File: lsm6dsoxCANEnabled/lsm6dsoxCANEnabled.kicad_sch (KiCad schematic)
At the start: 29 parts, among them J1 CANH and CANL, J2 GPIO, J3 Power, SW1 Nrst, SW2 BOOT0 selector, U2 TJA1051T, U3 STM32F103C8Tx, U4 AMS1117CD-3.3, Y1 Crystal_GND24

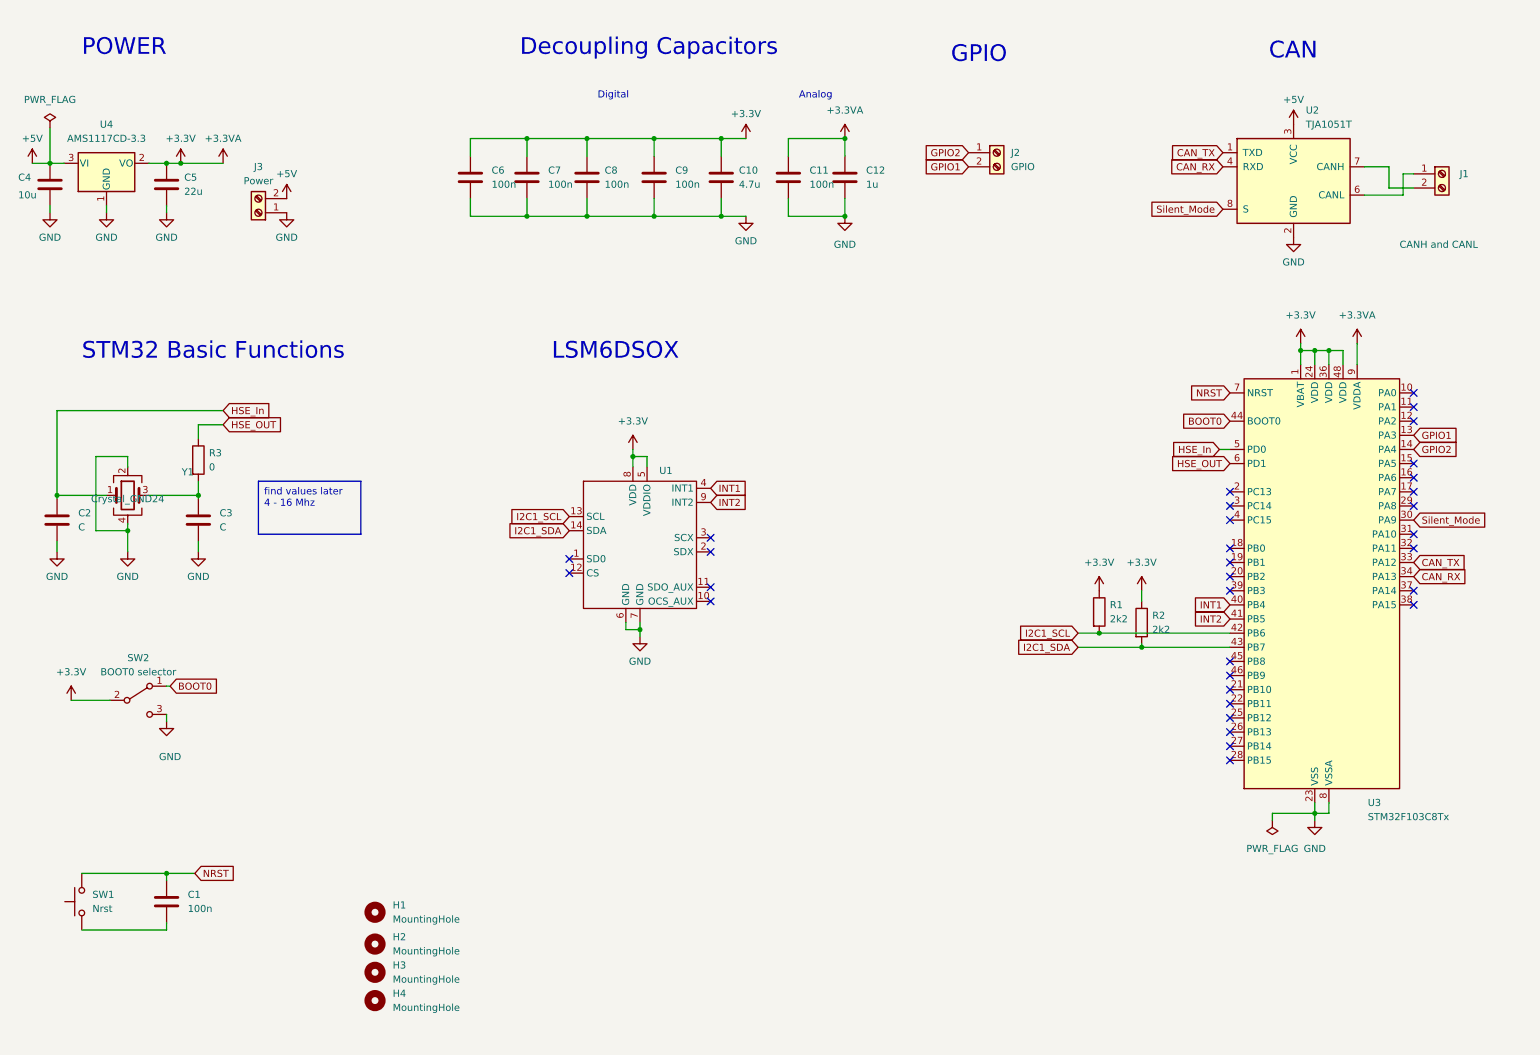
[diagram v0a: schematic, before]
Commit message: Started pcb with component placement and physical size constraints
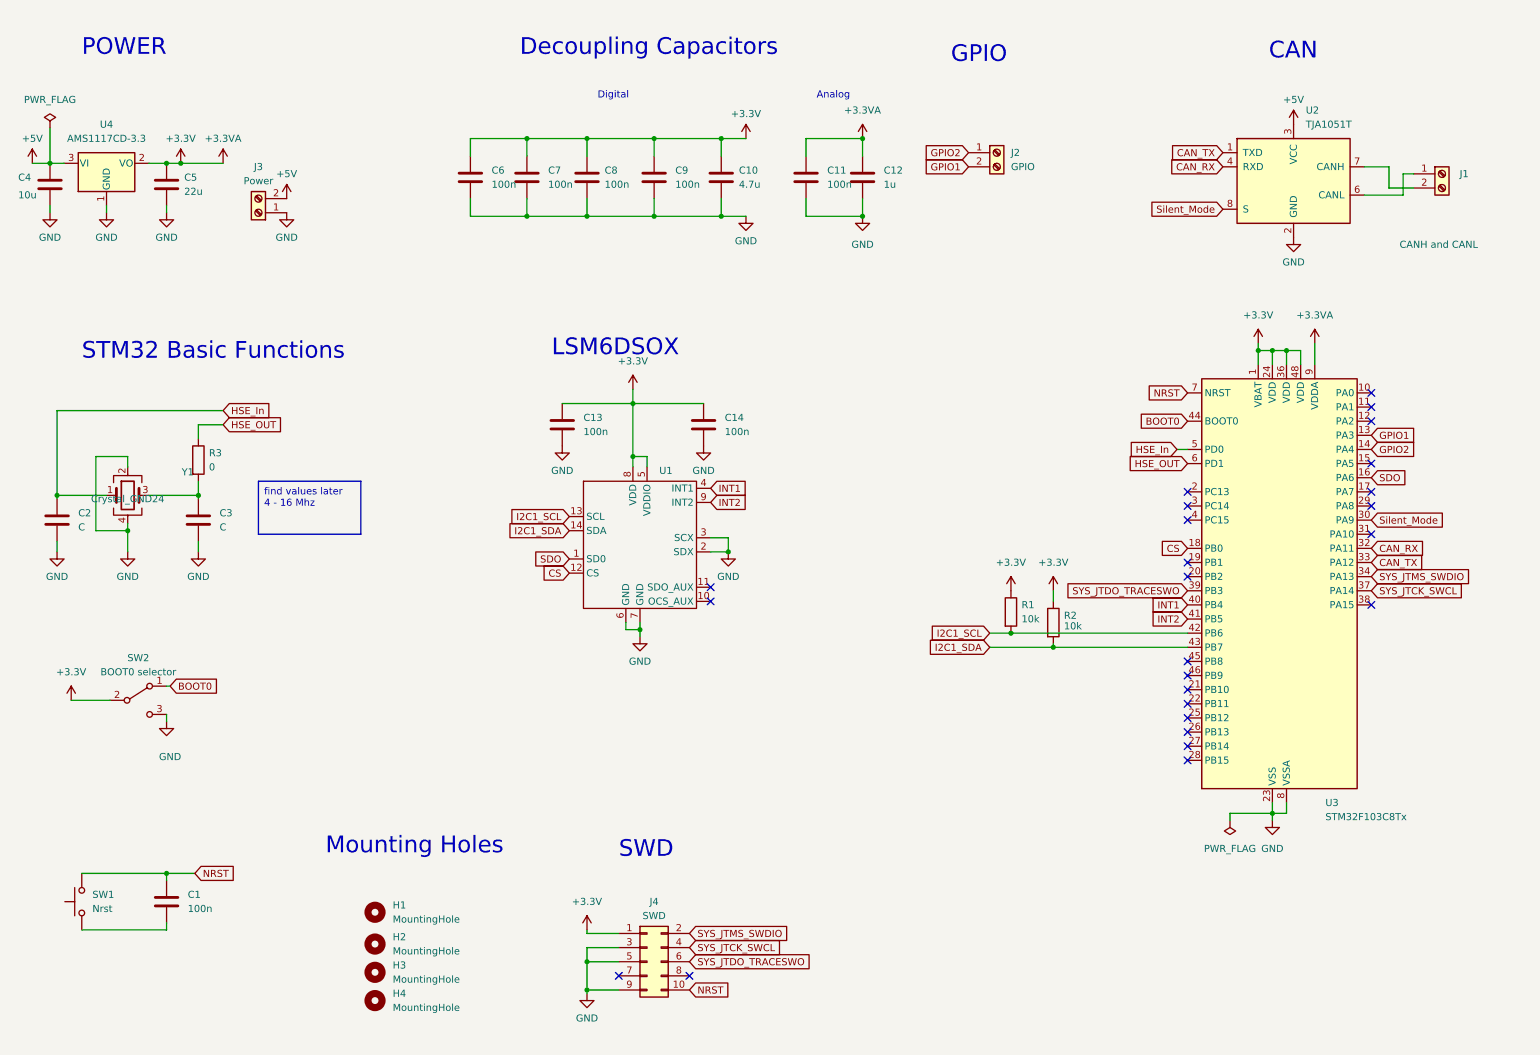
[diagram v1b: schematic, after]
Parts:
- added C13, C14: 100n, symbol Device:C
- added J4: SWD, symbol Connector_Generic:Conn_02x05_Odd_Even
- R1, R2: value 2k2 -> 10k
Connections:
- net +3.3V: now also C13.1, C14.1, J4.1 (Pin_1)
- net CAN_RX: now also U3.32 (PA11); no longer U3.34 (PA13)
- net GND: now also U1.2 (SDX), U1.3 (SCX), C13.2, C14.2, J4.3 (Pin_3), J4.5 (Pin_5), J4.9 (Pin_9)
- net NRST: now also J4.10 (Pin_10)
- net SDO: now reaches U3.16 (PA6)
- net SDO: now also U1.1 (SD0)
- net CS: now reaches U3.18 (PB0)
- net CS: now also U1.12 (CS)
- net SYS_JTCK_SWCL: now reaches U3.37 (PA14)
- net SYS_JTCK_SWCL: now also J4.4 (Pin_4)
- net SYS_JTDO_TRACESWO: now reaches U3.39 (PB3)
- net SYS_JTDO_TRACESWO: now also J4.6 (Pin_6)
- new net SYS_JTMS_SWDIO: J4.2 (Pin_2), U3.34 (PA13)
- no-connect marks 32 -> 25
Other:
- note added: "Mounting Holes"
- note added: "SWD"
- moved on the sheet: C11, C12, R1, R2, U3

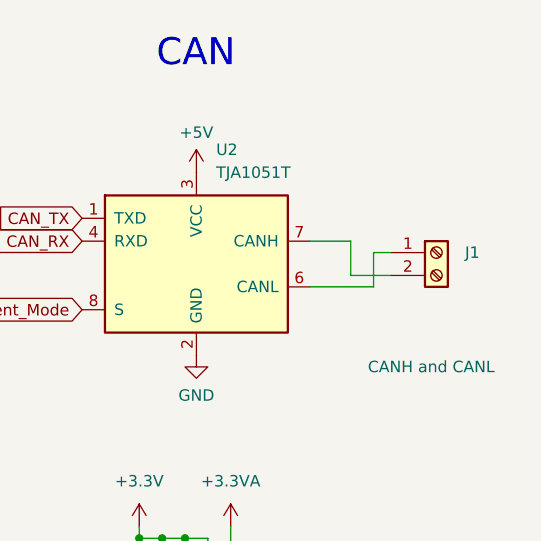
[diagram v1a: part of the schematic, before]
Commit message: started the routing process for the CAN LSM6DSOX
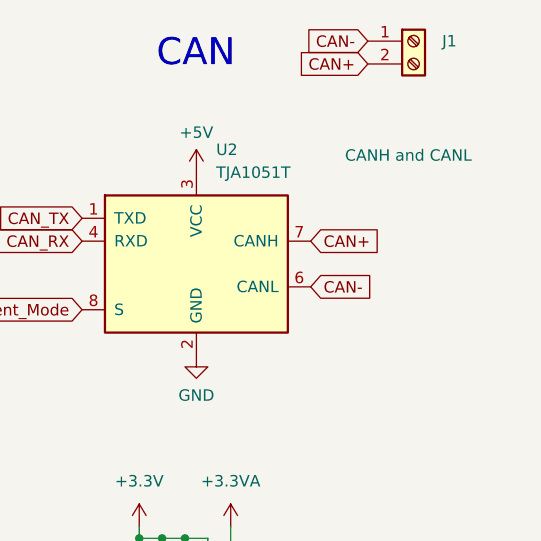
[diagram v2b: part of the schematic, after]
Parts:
- C13, C14: footprint (none) -> Capacitor_SMD:C_0603_1608Metric_Pad1.08x0.95mm_HandSolder
- J4: footprint (none) -> Connector_PinHeader_2.54mm:PinHeader_2x05_P2.54mm_Vertical
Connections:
- net CAN-: now reaches J1.1 (Pin_1), U2.6 (CANL)
- net CAN+: now reaches J1.2 (Pin_2), U2.7 (CANH)
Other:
- moved on the sheet: J1
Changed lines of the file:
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@@
-    (stroke (width 0) (type default))
-  )
-  (wire (pts (xy 266.7 44.45) (xy 271.145 44.45))
     (stroke (width 0) (type default))
   )
@@
     (stroke (width 0) (type default))
   )
-  (wire (pts (xy 269.24 45.72) (xy 269.24 41.91))
-    (stroke (width 0) (type default))
-  )
   (wire (pts (xy 245.745 73.66) (xy 245.745 76.2))
     (stroke (width 0) (type default))
@@
     (stroke (width 0) (type default))
   )
-  (wire (pts (xy 266.7 40.64) (xy 266.7 44.45))
-    (stroke (width 0) (type default))
-  )
   (wire (pts (xy 161.925 35.56) (xy 172.085 35.56))
     (stroke (width 0) (type default))
@@
     (stroke (width 0) (type default))
   )
-  (wire (pts (xy 262.255 40.64) (xy 266.7 40.64))
-    (stroke (width 0) (type default))
-  )
   (wire (pts (xy 206.375 127) (xy 230.505 127))
     (stroke (width 0) (type default))
@@
     (stroke (width 0) (type default))
   )
-  (wire (pts (xy 269.24 41.91) (xy 271.145 41.91))
-    (stroke (width 0) (type default))
-  )
   (wire (pts (xy 128.27 178.435) (xy 122.555 178.435))
     (stroke (width 0) (type default))
@@
   )
   (wire (pts (xy 27.305 109.855) (xy 27.305 107.95))
-    (stroke (width 0) (type default))
-  )
-  (wire (pts (xy 262.255 45.72) (xy 269.24 45.72))
     (stroke (width 0) (type default))
   )
@@
     )
   )
+  (global_label "CAN+" (shape input) (at 262.255 40.64 0) (fields_autoplaced)
+    (effects (font (size 1.27 1.27)) (justify left))
+    (property "Intersheetrefs" "${INTERSHEET_REFS}" (at 270.5017 40.64 0)
+      (effects (font (size 1.27 1.27)) (justify left) hide)
+    )
+  )
   (global_label "HSE_OUT" (shape input) (at 57.15 86.995 0) (fields_autoplaced)
     (effects (font (size 1.27 1.27)) (justify left))
@@
     )
   )
+  (global_label "CAN+" (shape input) (at 268.605 20.955 180) (fields_autoplaced)
+    (effects (font (size 1.27 1.27)) (justify right))
+    (property "Intersheetrefs" "${INTERSHEET_REFS}" (at 260.3583 20.955 0)
+      (effects (font (size 1.27 1.27)) (justify right) hide)
+    )
+  )
   (global_label "SYS_JTMS_SWDIO" (shape input) (at 263.525 114.3 0) (fields_autoplaced)
     (effects (font (size 1.27 1.27)) (justify left))
@@
     )
   )
+  (global_label "CAN-" (shape input) (at 268.605 18.415 180) (fields_autoplaced)
+    (effects (font (size 1.27 1.27)) (justify right))
+    (property "Intersheetrefs" "${INTERSHEET_REFS}" (at 260.3583 18.415 0)
+      (effects (font (size 1.27 1.27)) (justify right) hide)
+    )
+  )
   (global_label "NRST" (shape input) (at 52.07 167.64 0) (fields_autoplaced)
     (effects (font (size 1.27 1.27)) (justify left))
@@
     (property "Intersheetrefs" "${INTERSHEET_REFS}" (at 207.8047 116.84 0)
       (effects (font (size 1.27 1.27)) (justify right) hide)
+    )
+  )
+  (global_label "CAN-" (shape input) (at 262.255 45.72 0) (fields_autoplaced)
+    (effects (font (size 1.27 1.27)) (justify left))
+    (property "Intersheetrefs" "${INTERSHEET_REFS}" (at 270.5017 45.72 0)
+      (effects (font (size 1.27 1.27)) (justify left) hide)
     )
   )
@@
       (effects (font (size 1.27 1.27)) (justify left))
     )
-    (property "Footprint" "" (at 144.4752 90.805 0)
+    (property "Footprint" "Capacitor_SMD:C_0603_1608Metric_Pad1.08x0.95mm_HandSolder" (at 144.4752 90.805 0)
       (effects (font (size 1.27 1.27)) hide)
     )
@@
     )
   )
-  (symbol (lib_id "Connector:Screw_Terminal_01x02") (at 276.225 41.91 0) (unit 1)
+  (symbol (lib_id "Connector:Screw_Terminal_01x02") (at 273.685 18.415 0) (unit 1)
     (in_bom yes) (on_board yes) (dnp no)
-    (property "Reference" "J1" (at 279.4 41.91 0)
-      (effects (font (size 1.27 1.27)) (justify left))
-    )
-    (property "Value" "CANH and CANL " (at 268.605 54.61 0)
-      (effects (font (size 1.27 1.27)) (justify left))
-    )
-    (property "Footprint" "TerminalBlock_Phoenix:TerminalBlock_Phoenix_MKDS-1,5-2_1x02_P5.00mm_Horizontal" (at 276.225 41.91 0)
-      (effects (font (size 1.27 1.27)) hide)
-    )
-    (property "Datasheet" "~" (at 276.225 41.91 0)
+    (property "Reference" "J1" (at 276.86 18.415 0)
+      (effects (font (size 1.27 1.27)) (justify left))
+    )
+    (property "Value" "CANH and CANL " (at 266.065 31.115 0)
+      (effects (font (size 1.27 1.27)) (justify left))
+    )
+    (property "Footprint" "TerminalBlock_Phoenix:TerminalBlock_Phoenix_MKDS-1,5-2_1x02_P5.00mm_Horizontal" (at 273.685 18.415 0)
+      (effects (font (size 1.27 1.27)) hide)
+    )
+    (property "Datasheet" "~" (at 273.685 18.415 0)
       (effects (font (size 1.27 1.27)) hide)
     )
@@
       (effects (font (size 1.27 1.27)) (justify left))
     )
-    (property "Footprint" "" (at 119.0752 90.805 0)
+    (property "Footprint" "Capacitor_SMD:C_0603_1608Metric_Pad1.08x0.95mm_HandSolder" (at 119.0752 90.805 0)
       (effects (font (size 1.27 1.27)) hide)
     )
@@
       (effects (font (size 1.27 1.27)))
     )
-    (property "Footprint" "" (at 133.35 183.515 0)
-      (effects (font (size 1.27 1.27)) hide)
-    )
+    (property "Footprint" "Connector_PinHeader_2.54mm:PinHeader_2x05_P2.54mm_Vertical" (at 133.35 183.515 0)
+      (effects (font (size 1.27 1.27)) hide)
+    )

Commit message: decided to connect 5V connections directly instead of making a power plane. Probably should change this later
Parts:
- added R4: 120, Resistor_SMD:R_0603_1608Metric_Pad0.98x0.95mm_HandSolder, symbol Device:R_Small
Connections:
- net CAN+: now also R4.2
- net CAN-: now also R4.1
- net GND: now also C1.2, SW1.1
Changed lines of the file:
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@@
   (junction (at 46.99 40.005) (diameter 0) (color 0 0 0 0)
   )
+  (junction (at 31.75 177.8) (diameter 0) (color 0 0 0 0)
+  )
   (junction (at 27.305 99.695) (diameter 0) (color 0 0 0 0)
   )
@@
   (junction (at 146.685 35.56) (diameter 0) (color 0 0 0 0)
   )
+  (junction (at 263.525 22.225) (diameter 0) (color 0 0 0 0)
+  )
   (junction (at 40.005 106.045) (diameter 0) (color 0 0 0 0)
   )
@@
   )
   (junction (at 146.685 49.53) (diameter 0) (color 0 0 0 0)
+  )
+  (junction (at 263.525 17.145) (diameter 0) (color 0 0 0 0)
   )
   (junction (at 245.745 156.845) (diameter 0) (color 0 0 0 0)
@@
     (stroke (width 0) (type default))
   )
+  (wire (pts (xy 263.525 22.225) (xy 266.065 22.225))
+    (stroke (width 0) (type default))
+  )
   (wire (pts (xy 130.81 80.645) (xy 130.81 83.185))
     (stroke (width 0) (type default))
@@
     (stroke (width 0) (type default))
   )
+  (wire (pts (xy 263.525 22.225) (xy 262.255 22.225))
+    (stroke (width 0) (type default))
+  )
   (wire (pts (xy 27.305 100.33) (xy 27.305 99.695))
     (stroke (width 0) (type default))
@@
     (stroke (width 0) (type default))
   )
+  (wire (pts (xy 31.75 180.975) (xy 31.75 177.8))
+    (stroke (width 0) (type default))
+  )
   (wire (pts (xy 34.29 106.045) (xy 40.005 106.045))
     (stroke (width 0) (type default))
@@
     (stroke (width 0) (type default))
   )
+  (wire (pts (xy 266.065 17.145) (xy 266.065 18.415))
+    (stroke (width 0) (type default))
+  )
   (wire (pts (xy 52.705 97.155) (xy 52.705 99.695))
     (stroke (width 0) (type default))
@@
     (stroke (width 0) (type default))
   )
+  (wire (pts (xy 266.065 22.225) (xy 266.065 20.955))
+    (stroke (width 0) (type default))
+  )
+  (wire (pts (xy 266.065 20.955) (xy 268.605 20.955))
+    (stroke (width 0) (type default))
+  )
   (wire (pts (xy 248.285 73.66) (xy 248.285 76.2))
     (stroke (width 0) (type default))
@@
     (stroke (width 0) (type default))
   )
+  (wire (pts (xy 263.525 17.145) (xy 266.065 17.145))
+    (stroke (width 0) (type default))
+  )
   (wire (pts (xy 26.035 33.655) (xy 26.035 40.005))
     (stroke (width 0) (type default))
@@
     (stroke (width 0) (type default))
   )
+  (wire (pts (xy 266.065 18.415) (xy 268.605 18.415))
+    (stroke (width 0) (type default))
+  )
   (wire (pts (xy 228.6 91.44) (xy 230.505 91.44))
     (stroke (width 0) (type default))
@@
   )
   (wire (pts (xy 47.625 133.985) (xy 46.99 133.985))
+    (stroke (width 0) (type default))
+  )
+  (wire (pts (xy 263.525 17.145) (xy 262.255 17.145))
     (stroke (width 0) (type default))
   )
@@
     )
   )
-  (global_label "CAN+" (shape input) (at 268.605 20.955 180) (fields_autoplaced)
-    (effects (font (size 1.27 1.27)) (justify right))
-    (property "Intersheetrefs" "${INTERSHEET_REFS}" (at 260.3583 20.955 0)
+  (global_label "CAN+" (shape input) (at 262.255 22.225 180) (fields_autoplaced)
+    (effects (font (size 1.27 1.27)) (justify right))
+    (property "Intersheetrefs" "${INTERSHEET_REFS}" (at 254.0083 22.225 0)
       (effects (font (size 1.27 1.27)) (justify right) hide)
     )
@@
     )
   )
-  (global_label "CAN-" (shape input) (at 268.605 18.415 180) (fields_autoplaced)
-    (effects (font (size 1.27 1.27)) (justify right))
-    (property "Intersheetrefs" "${INTERSHEET_REFS}" (at 260.3583 18.415 0)
+  (global_label "CAN-" (shape input) (at 262.255 17.145 180) (fields_autoplaced)
+    (effects (font (size 1.27 1.27)) (justify right))
+    (property "Intersheetrefs" "${INTERSHEET_REFS}" (at 254.0083 17.145 0)
       (effects (font (size 1.27 1.27)) (justify right) hide)
     )
@@
     )
   )
+  (symbol (lib_id "Device:R_Small") (at 263.525 19.685 0) (unit 1)
+    (in_bom yes) (on_board yes) (dnp no)
+    (property "Reference" "R4" (at 262.255 19.685 0)
+      (effects (font (size 1.27 1.27)) (justify left))
+    )
+    (property "Value" "120" (at 265.43 19.685 0)
+      (effects (font (size 1.27 1.27)) (justify left))
+    )
+    (property "Footprint" "Resistor_SMD:R_0603_1608Metric_Pad0.98x0.95mm_HandSolder" (at 263.525 19.685 0)
+      (effects (font (size 1.27 1.27)) hide)
+    )
+    (property "Datasheet" "~" (at 263.525 19.685 0)
+      (effects (font (size 1.27 1.27)) hide)
+    )
+    (pin "1")
+    (pin "2")
+    (instances
+      (project "lsm6dsoxCANEnabled"
+        (path "/bd29ea80-b13c-4b12-a75c-c0e3a78dbfa4"
+          (reference "R4") (unit 1)
+        )
+      )
+    )
+  )
   (symbol (lib_id "Connector:Screw_Terminal_01x02") (at 196.215 38.1 0) (unit 1)
     (in_bom yes) (on_board yes) (dnp no) (fields_autoplaced)
@@
         )
       )
+    )
+  )
+  (symbol (lib_id "power:GND") (at 31.75 180.975 0) (unit 1)
+    (in_bom yes) (on_board yes) (dnp no) (fields_autoplaced)
+    (property "Reference" "#PWR032" (at 31.75 187.325 0)
+      (effects (font (size 1.27 1.27)) hide)
+    )
+    (property "Value" "GND" (at 31.75 186.055 0)
+      (effects (font (size 1.27 1.27)))
+    )
+    (property "Footprint" "" (at 31.75 180.975 0)
+      (effects (font (size 1.27 1.27)) hide)
+    )
+    (property "Datasheet" "" (at 31.75 180.975 0)
+      (effects (font (size 1.27 1.27)) hide)
+    )
+    (pin "1")
+    (instances
+      (project "lsm6dsoxCANEnabled"
+        (path "/bd29ea80-b13c-4b12-a75c-c0e3a78dbfa4"
+          (reference "#PWR032") (unit 1)
+        )
+      )

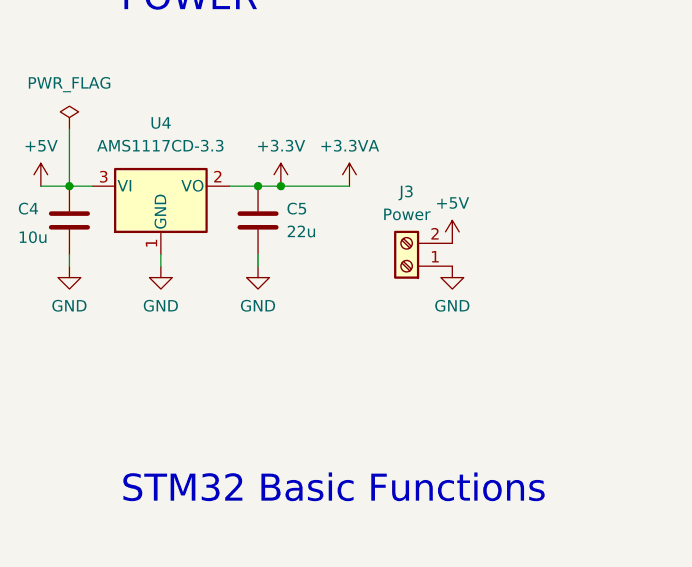
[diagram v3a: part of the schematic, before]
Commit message: added DFR logo,revision number, and the current date
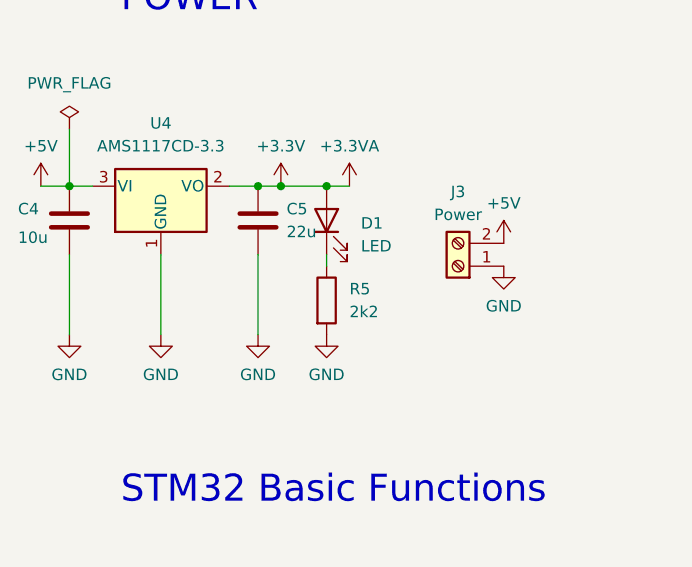
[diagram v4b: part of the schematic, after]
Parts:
- added D1: LED, LED_SMD:LED_0603_1608Metric_Pad1.05x0.95mm_HandSolder, symbol Device:LED
- added R5: 2k2, Resistor_SMD:R_0603_1608Metric_Pad0.98x0.95mm_HandSolder, symbol Device:R
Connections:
- net +3.3V: now also D1.2 (A)
- net GND: now also R5.2
- new net: D1.1 (K), R5.1
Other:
- moved on the sheet: J3

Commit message: updated some stuff
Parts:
- removed J1: CANH and CANL, TerminalBlock_Phoenix:TerminalBlock_Phoenix_MKDS-1,5-2_1x02_P5.00mm_Horizontal, symbol Connector:Screw_Terminal_01x02
- added J5: CANH and CANL input n output, TerminalBlock_Phoenix:TerminalBlock_Phoenix_MKDS-1,5-4_1x04_P5.00mm_Horizontal, symbol Connector:Screw_Terminal_01x04
- SW2: value BOOT0 selector -> BOOT0
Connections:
- net +3.3V: now also SW2.1 (A); no longer SW2.2 (B)
- net BOOT0: now also SW2.2 (B); no longer SW2.1 (A)
- net CAN+: now also J5.1 (Pin_1), J5.4 (Pin_4)
- net CAN-: now also J5.2 (Pin_2), J5.3 (Pin_3)
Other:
- moved on the sheet: R4
